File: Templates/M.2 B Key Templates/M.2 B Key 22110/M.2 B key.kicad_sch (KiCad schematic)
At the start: 2 parts

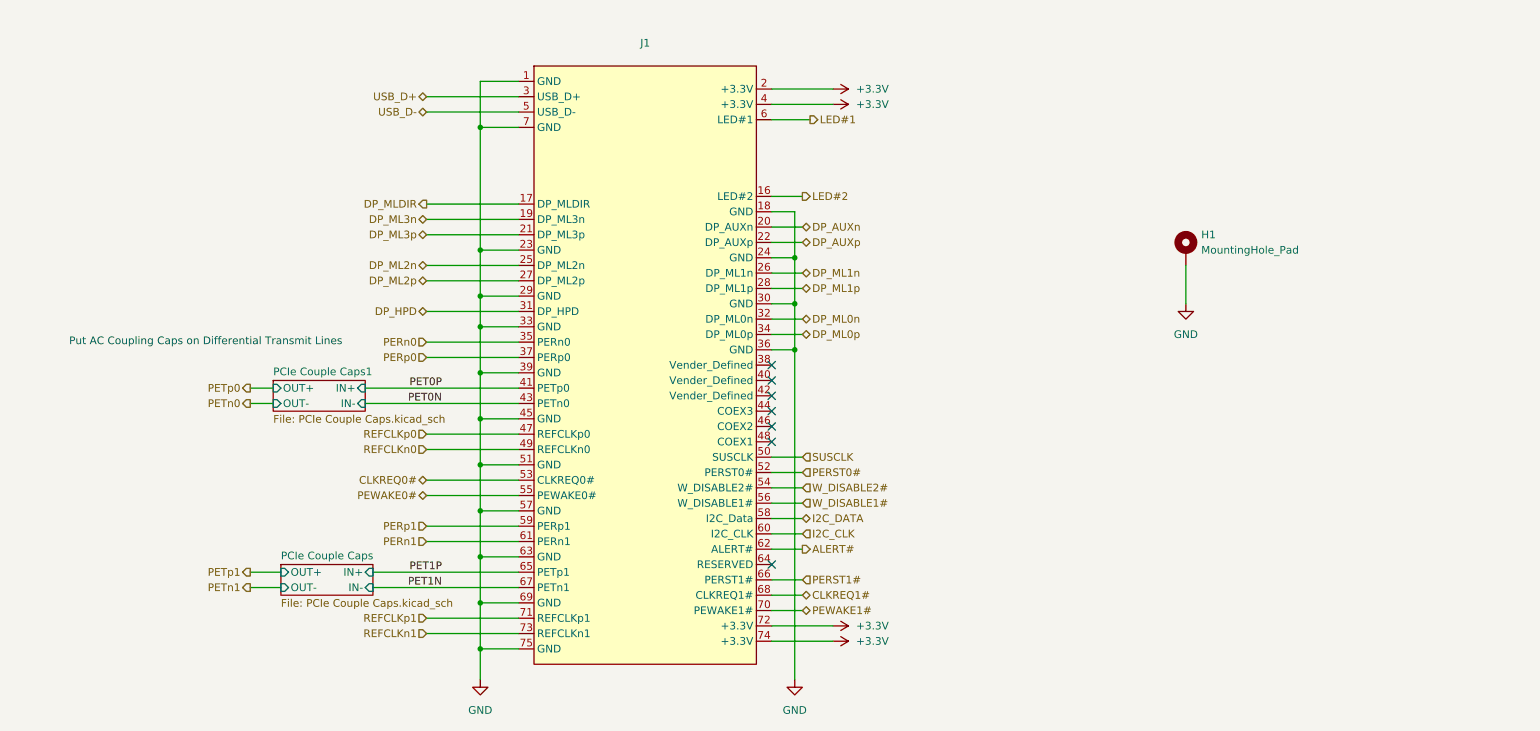
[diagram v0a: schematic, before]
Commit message: Added B Key Templates
-added B key Templates for all sizes
-corrected B key symbol pinout
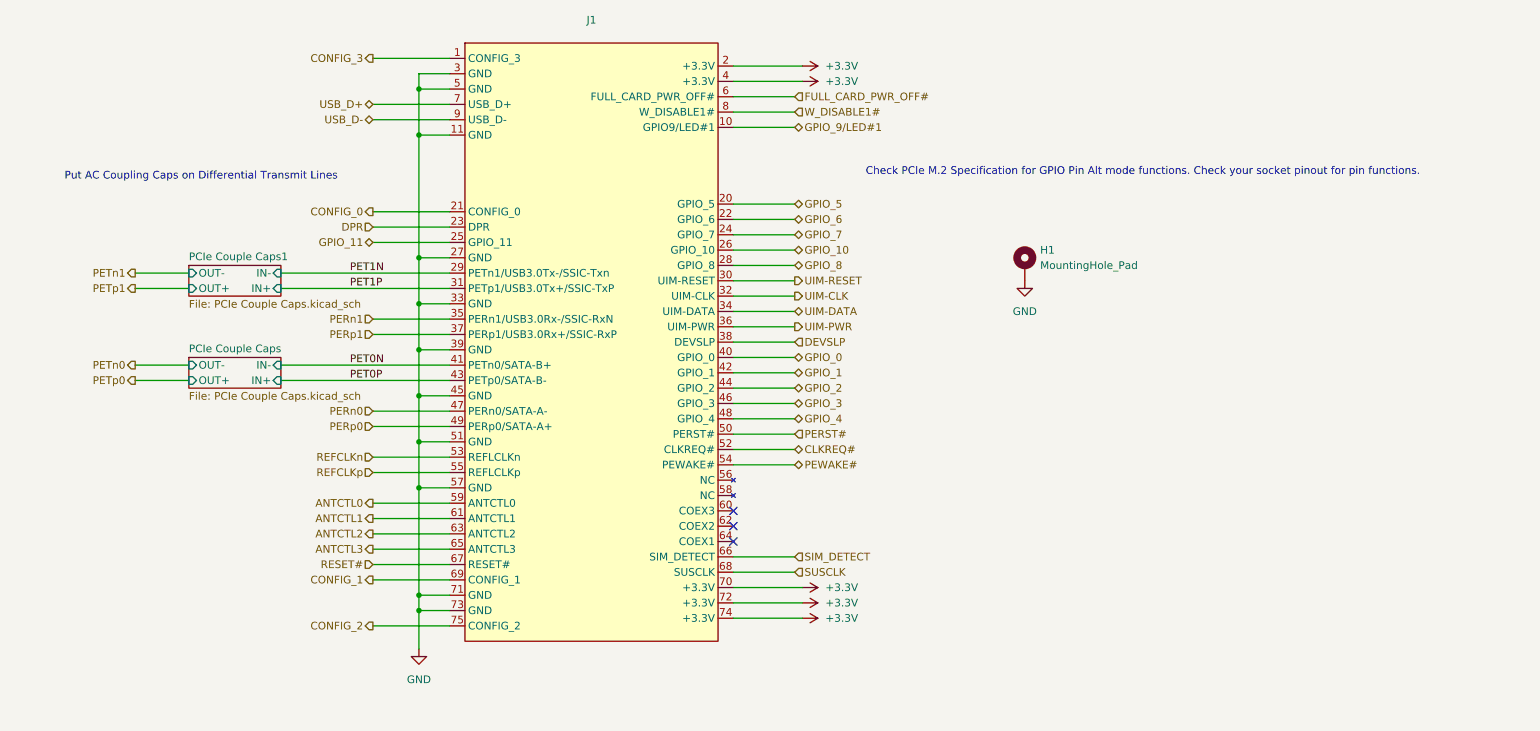
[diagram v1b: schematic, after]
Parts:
- removed J1: ~, PCIexpress:M.2 A Key Connector, symbol PCIexpress:M.2_A_Key
- added J1: ~, PCIexpress:M.2 B Key Connector, symbol PCIexpress:M.2_B_Key
- H1: footprint PCIexpress:M.2 Mounting Pad -> Athena KiCAd library:M.2 Mounting Pad
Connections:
- net +3.3V: now also J1.2 (+3.3V), J1.4 (+3.3V), J1.70 (+3.3V), J1.72 (+3.3V), J1.74 (+3.3V)
- net GND: now also J1.11 (GND), J1.27 (GND), J1.3 (GND), J1.33 (GND), J1.39 (GND), J1.45 (GND), J1.5 (GND), J1.51 (GND), J1.57 (GND), J1.71 (GND), J1.73 (GND)
- net PERn0: now also J1.47 (PERn0/SATA-A-)
- net PERn1: now also J1.35 (PERn1/USB3.0Rx-/SSIC-RxN)
- net PERp0: now also J1.49 (PERp0/SATA-A+)
- net PERp1: now also J1.37 (PERp1/USB3.0Rx+/SSIC-RxP)
- net PET0N: now also J1.41 (PETn0/SATA-B+)
- net PET0P: now also J1.43 (PETp0/SATA-B-)
- net PET1N: now also J1.29 (PETn1/USB3.0Tx-/SSIC-Txn)
- net PET1P: now also J1.31 (PETp1/USB3.0Tx+/SSIC-TxP)
- net SUSCLK: now also J1.68 (SUSCLK)
- net USB_D+: now also J1.7 (USB_D+)
- net USB_D-: now also J1.9 (USB_D-)
- net W_DISABLE1#: now also J1.8 (W_DISABLE1#)
- new net ANTCTL0: J1.59 (ANTCTL0)
- new net ANTCTL1: J1.61 (ANTCTL1)
- new net ANTCTL2: J1.63 (ANTCTL2)
- new net ANTCTL3: J1.65 (ANTCTL3)
- new net CLKREQ#: J1.52 (CLKREQ#)
- new net CONFIG_0: J1.21 (CONFIG_0)
- new net CONFIG_1: J1.69 (CONFIG_1)
- new net CONFIG_2: J1.75 (CONFIG_2)
- new net CONFIG_3: J1.1 (CONFIG_3)
- new net DEVSLP: J1.38 (DEVSLP)
- new net DPR: J1.23 (DPR)
- new net FULL_CARD_PWR_OFF#: J1.6 (FULL_CARD_PWR_OFF#)
- new net GPIO_0: J1.40 (GPIO_0)
- new net GPIO_1: J1.42 (GPIO_1)
- new net GPIO_10: J1.26 (GPIO_10)
- new net GPIO_11: J1.25 (GPIO_11)
- new net GPIO_2: J1.44 (GPIO_2)
- new net GPIO_3: J1.46 (GPIO_3)
- new net GPIO_4: J1.48 (GPIO_4)
- new net GPIO_5: J1.20 (GPIO_5)
- new net GPIO_6: J1.22 (GPIO_6)
- new net GPIO_7: J1.24 (GPIO_7)
- new net GPIO_8: J1.28 (GPIO_8)
- new net GPIO_9/LED#1: J1.10 (GPIO9/LED#1)
- new net PERST#: J1.50 (PERST#)
- new net PEWAKE#: J1.54 (PEWAKE#)
- new net REFCLKn: J1.53 (REFLCLKn)
- new net REFCLKp: J1.55 (REFLCLKp)
- new net RESET#: J1.67 (RESET#)
- new net SIM_DETECT: J1.66 (SIM_DETECT)
- new net UIM-CLK: J1.32 (UIM-CLK)
- new net UIM-DATA: J1.34 (UIM-DATA)
- new net UIM-PWR: J1.36 (UIM-PWR)
- new net UIM-RESET: J1.30 (UIM-RESET)
- no-connect marks 7 -> 3
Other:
- note added: "Check PCIe M.2 Specification for GPIO Pin Alt mode functions. Check your socket pinout for pin functions."
